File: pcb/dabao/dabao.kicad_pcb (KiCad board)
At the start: 2 copper layers, 127.4 x 114.6 mm, 75 parts, among them J1 Conn_01x05, J2 USB_C_Receptacle_USB2.0_16P, J3 Conn_01x04, J4 MagConn_01x04_Pin, J5 Conn_Battery, J7 Conn_01x04, J8 Display, SW1 SW_RESET, SW2 SW_POWER, U1 nice_nano, U2 MCP23017_SP

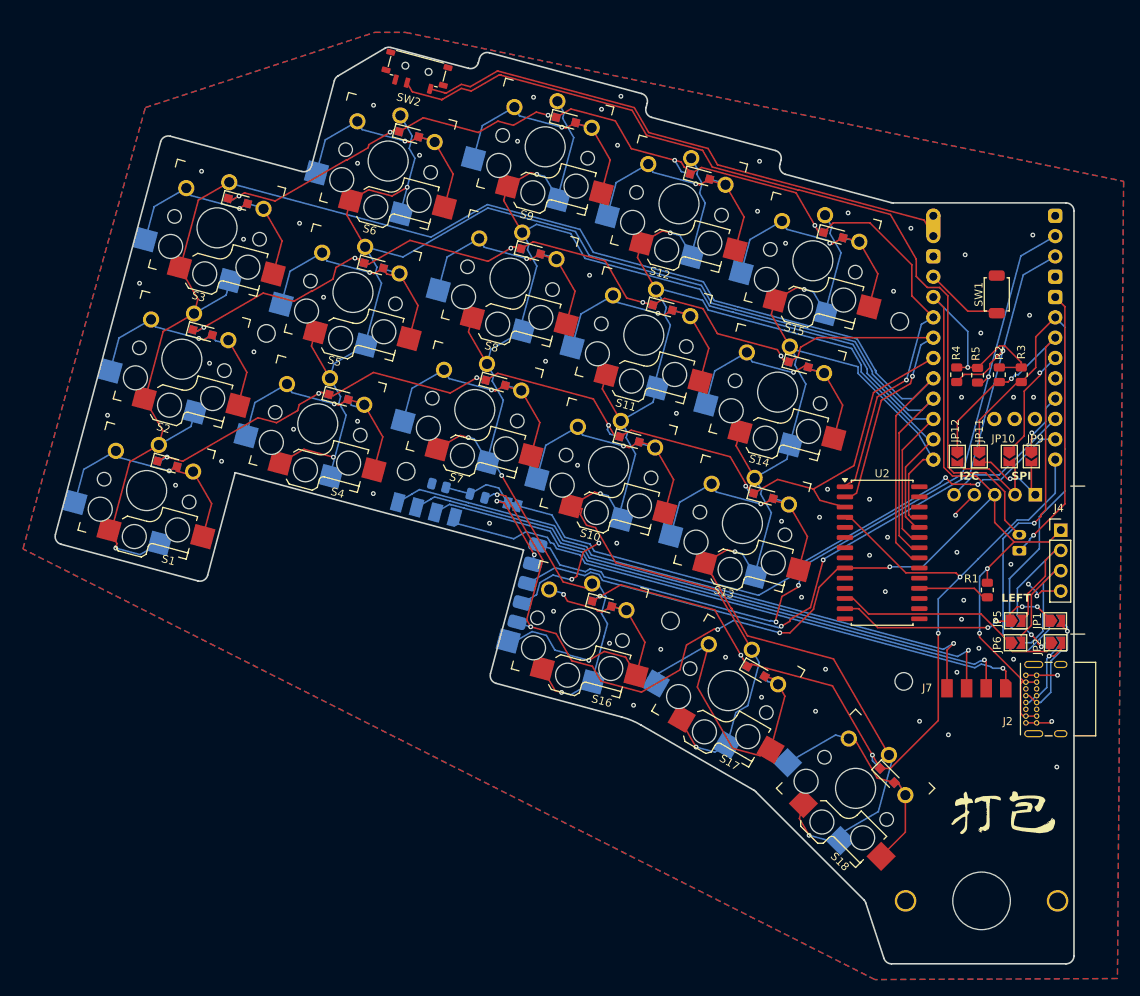
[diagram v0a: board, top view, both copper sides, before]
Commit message: Revert power switch back to original position, update to kicad 10
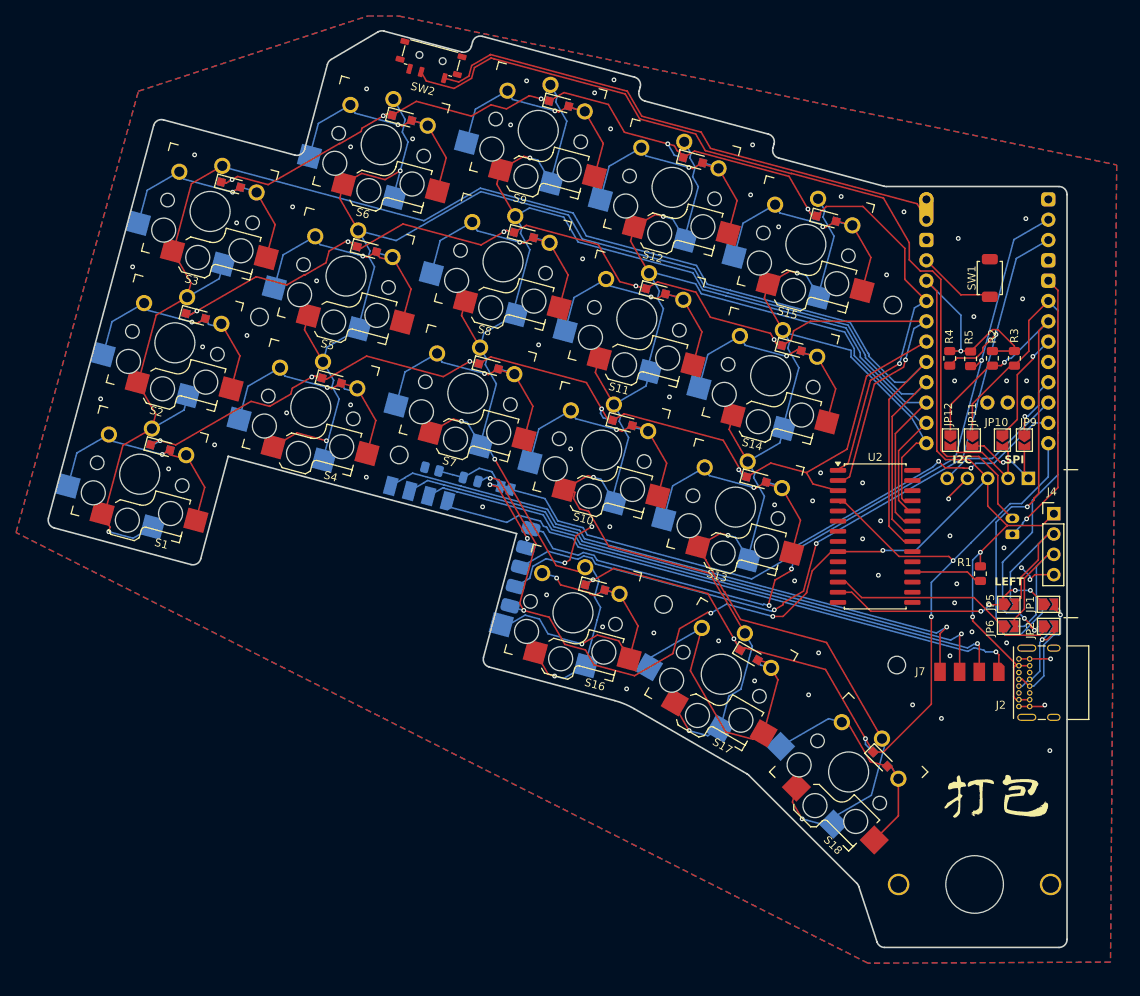
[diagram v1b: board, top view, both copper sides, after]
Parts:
- moved G*** 2.22 mm to (198.2, 134.5)
- moved D11 2.22 mm to (155.9, 71.6)
- moved D12 2.22 mm to (160.5, 55.2)
- moved D6 2.22 mm to (124.2, 49.9)
- moved J5 2.22 mm to (200.5, 102.0)
- moved JP1 2.22 mm to (205.0, 110.7)
- moved JP11 2.22 mm to (195.5, 90.2)
- moved JP2 2.22 mm to (205.0, 113.5)
- moved JP3 2.22 mm to (204.9, 110.7)
- moved R4 2.22 mm to (192.6, 80.0)
- moved R5 2.22 mm to (195.3, 80.0)
- moved REF** 2.22 mm to (156.9, 110.7)
- moved S13 2.22 mm to (165.9, 98.6)
- moved SW1 2.22 mm to (197.7, 69.9)
- moved D1 2.22 mm to (94.0, 91.1)
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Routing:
- net /BAT+: track 70.1 -> 67.8 mm
- net Net-(J5-Pin_2): track 116.4 -> 114.4 mm

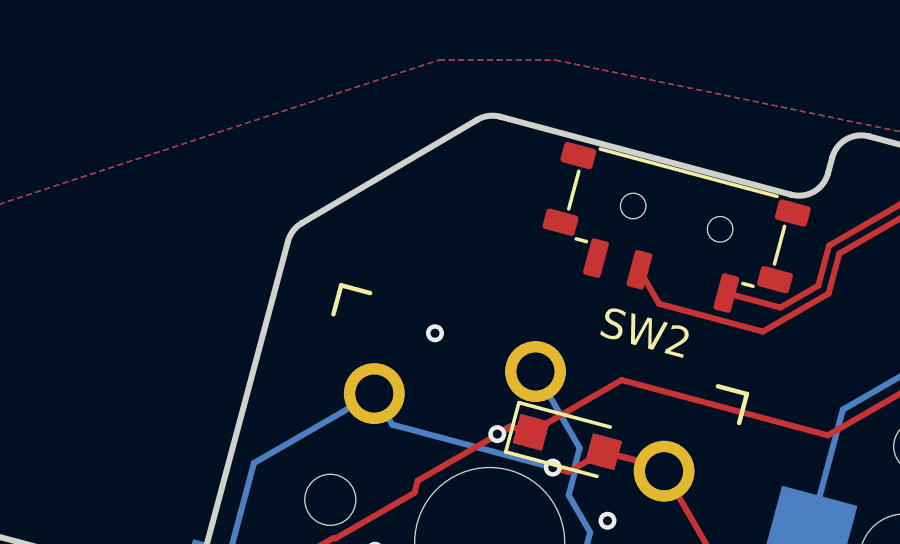
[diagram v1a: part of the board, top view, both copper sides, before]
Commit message: Add back mounting hole
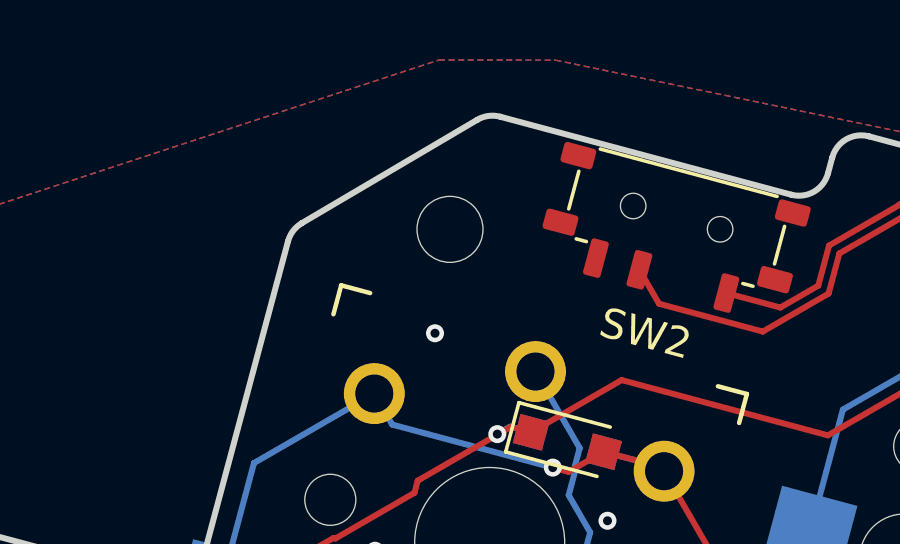
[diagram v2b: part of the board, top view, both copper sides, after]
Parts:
- added REF**: MountingHole_2.2mm_M2, MountingHole:MountingHole_2.2mm_M2, F.Cu at (120.3, 42.8)
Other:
- board text added: "jmklam v1.1"
- board text removed: "jmklam v1.0"
